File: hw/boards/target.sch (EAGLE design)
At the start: 21 parts, among them T1 771-BC847BS-T/R, U1 579-MCP1703T-3002ECB, U2 771-LPC824M201JDH20J, U4 579-MCP6291T-E/OT, X1 798-DF134P125V20

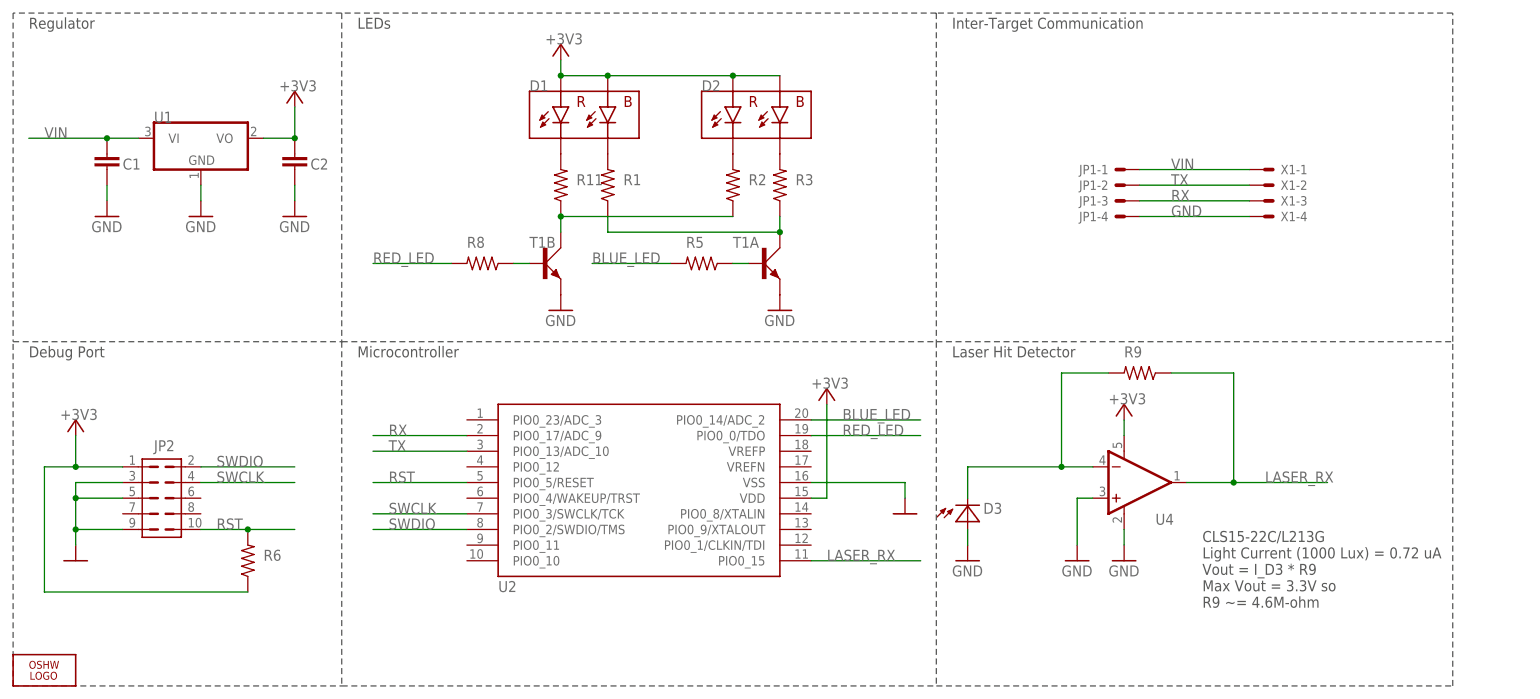
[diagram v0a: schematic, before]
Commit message: Cleanup some parts, generate BOM.
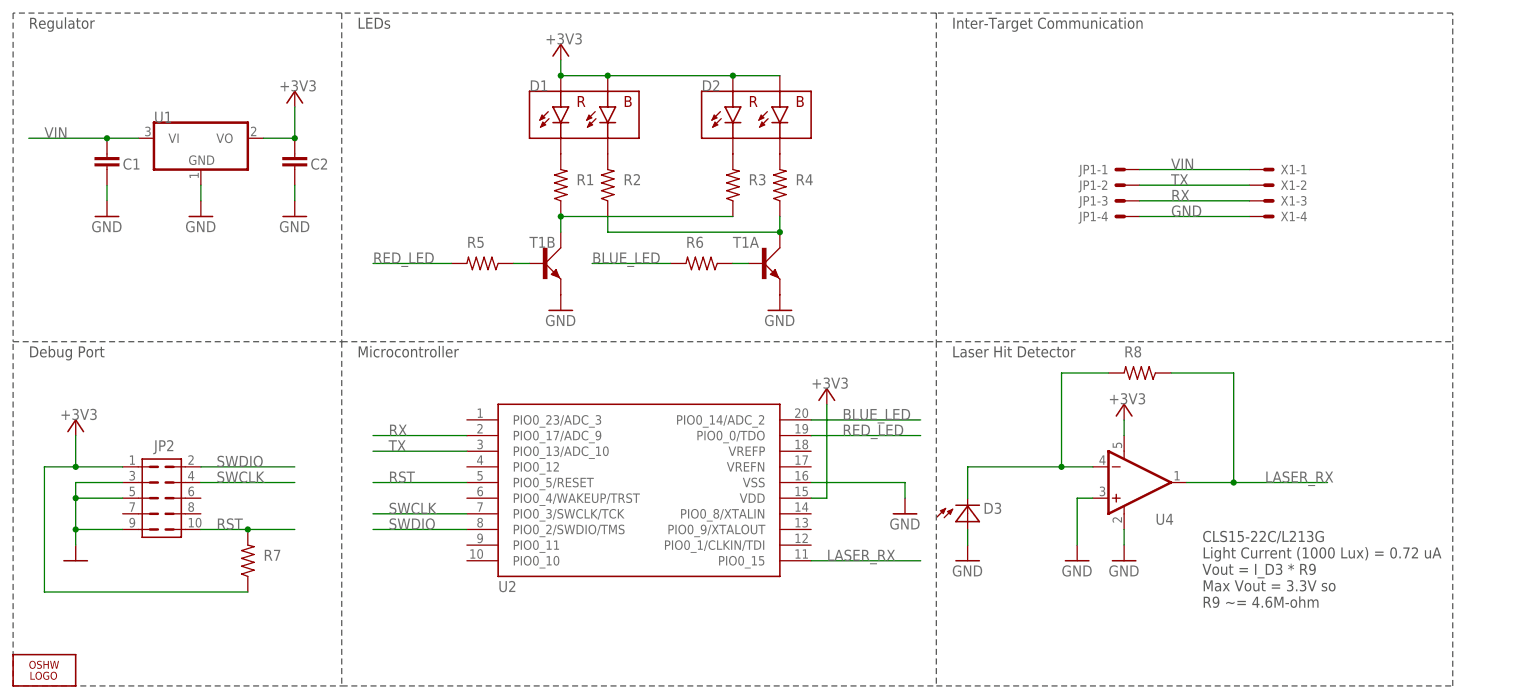
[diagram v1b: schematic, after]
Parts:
- removed R11: 71-CRCW060368R0FKEB, rcl:R-US_R0603
- removed R9: 71-CRCW06034M64FKEA, rcl:R-US_R0603
- added R4: 71-CRCW0603-5.6-E3, rcl:R-US_R0603
- added R7: 71-CRCW0603-10K-E3, rcl:R-US_R0603
- R1, R3: value 71-CRCW0603-5.6-E3 -> 71-CRCW060368R0FKEB
- R2: value 71-CRCW060368R0FKEB -> 71-CRCW0603-5.6-E3
- R6: value 71-CRCW0603-10K-E3 -> 71-CRCW0603220RFKEB
- R8: value 71-CRCW0603220RFKEB -> 71-CRCW06034M64FKEA
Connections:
- net +3V3: now also R7.1; no longer R6.1
- net BLUE_LED: now also R6.2; no longer R5.2
- net LASER_RX: now also R8.1; no longer R9.1
- net N$1: now also R2.1, R4.1; no longer R1.1, R3.1
- net N$11: now also R5.1; no longer R8.1
- net N$2: now also R1.1, R3.1; no longer R11.1, R2.1
- net N$3: now also R1.2; no longer R11.2
- net N$4: now also R6.1; no longer R5.1
- net N$5: now also R8.2; no longer R9.2
- net N$6: now also R3.2; no longer R2.2
- net N$7: now also R2.2; no longer R1.2
- net N$8: now also R4.2; no longer R3.2
- net RED_LED: now also R5.2; no longer R8.2
- net RST: now also R7.2; no longer R6.2
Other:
- moved on the sheet: R1, R2, R3, R5, R6, R8

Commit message: Fix some part numbers
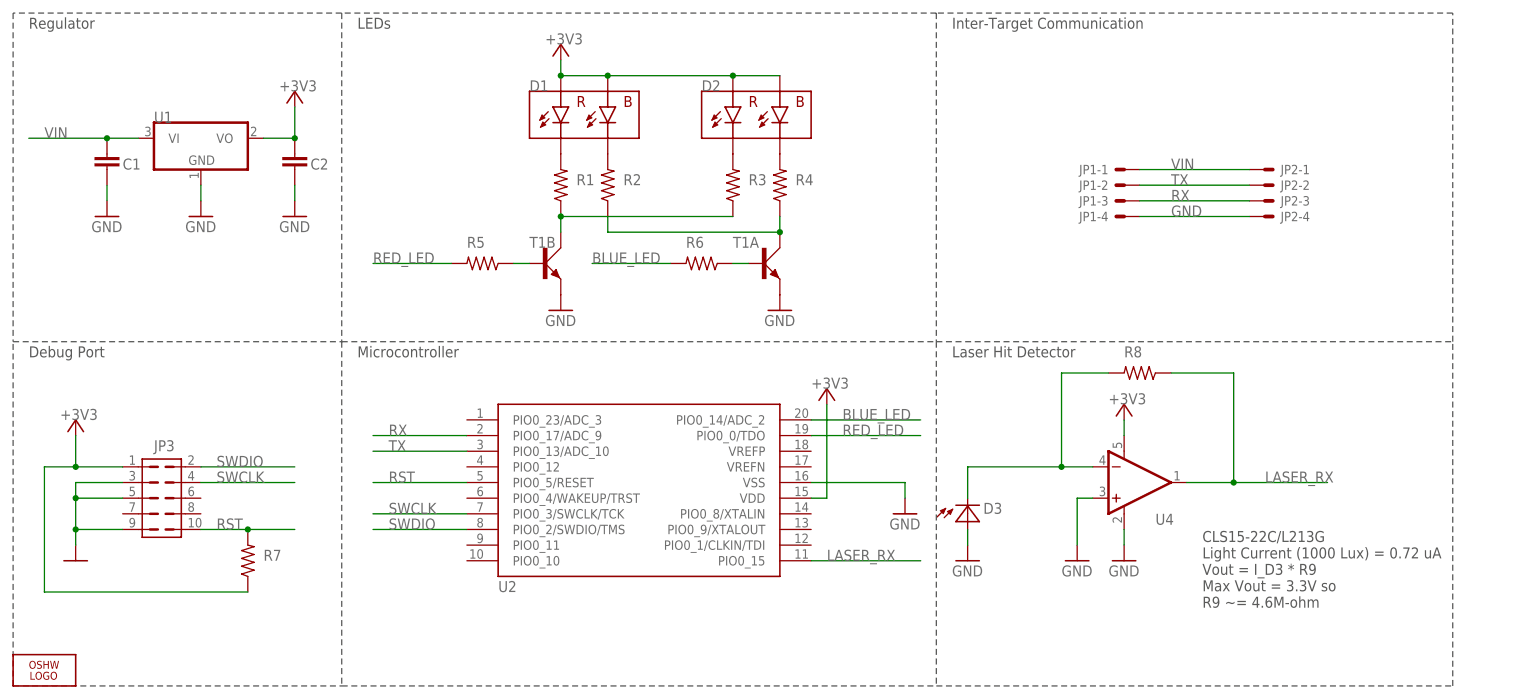
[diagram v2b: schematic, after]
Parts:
- removed X1: 798-DF134P125V20, con-molex:53398-04
- added JP3: FTSH-105-01-L, torpedo:FTSH-105
- JP2: value FTSH-105-01-L -> 798-DF134P125V20; device torpedo:FTSH-105 -> con-molex:53398-04
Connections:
- net +3V3: now also JP3.1; no longer JP2.1
- net GND: now also JP2-4.S, JP3.3, JP3.5, JP3.9; no longer JP2.3, JP2.5, JP2.9, X1-4.S
- net RST: now also JP3.10; no longer JP2.10
- net RX: now also JP2-3.S; no longer X1-3.S
- net SWCLK: now also JP3.4; no longer JP2.4
- net SWDIO: now also JP3.2; no longer JP2.2
- net TX: now also JP2-2.S; no longer X1-2.S
- net VIN: now also JP2-1.S; no longer X1-1.S
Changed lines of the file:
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@@
 <part name="R1" library="rcl" deviceset="R-US_" device="R0603" value="71-CRCW060368R0FKEB"/>
 <part name="T1" library="transistor-small-signal" deviceset="BC847BS" device="" value="771-BC847BS-T/R"/>
-<part name="X1" library="con-molex" deviceset="53?-04" device="398" value="798-DF134P125V20"/>
+<part name="JP2" library="con-molex" deviceset="53?-04" device="398" value="798-DF134P125V20"/>
 <part name="JP1" library="con-molex" deviceset="53?-04" device="398" value="798-DF134P125V20"/>
 <part name="LOGO2" library="ohw-logo" deviceset="OSHW_LOGO_FILL" device="X0150-NT"/>
@@
 <part name="GND8" library="supply1" deviceset="GND" device=""/>
 <part name="+3V31" library="supply1" deviceset="+3V3" device=""/>
-<part name="JP2" library="torpedo" deviceset="FTSH-105" device="" value="FTSH-105-01-L"/>
+<part name="JP3" library="torpedo" deviceset="FTSH-105" device="" value="FTSH-105-01-L"/>
 <part name="R7" library="rcl" deviceset="R-US_" device="R0603" value="71-CRCW0603-10K-E3"/>
 <part name="GND3" library="supply1" deviceset="GND" device=""/>
@@
 <attribute name="NAME" x="83.82" y="71.12" size="1.778" layer="95"/>
 </instance>
-<instance part="X1" gate="-1" x="203.2" y="83.82" smashed="yes">
+<instance part="JP2" gate="-1" x="203.2" y="83.82" smashed="yes">
 <attribute name="NAME" x="205.74" y="83.058" size="1.524" layer="95"/>
 </instance>
-<instance part="X1" gate="-2" x="203.2" y="81.28" smashed="yes">
+<instance part="JP2" gate="-2" x="203.2" y="81.28" smashed="yes">
 <attribute name="NAME" x="205.74" y="80.518" size="1.524" layer="95"/>
 </instance>
-<instance part="X1" gate="-3" x="203.2" y="78.74" smashed="yes">
+<instance part="JP2" gate="-3" x="203.2" y="78.74" smashed="yes">
 <attribute name="NAME" x="205.74" y="77.978" size="1.524" layer="95"/>
 </instance>
-<instance part="X1" gate="-4" x="203.2" y="76.2" smashed="yes">
+<instance part="JP2" gate="-4" x="203.2" y="76.2" smashed="yes">
 <attribute name="NAME" x="205.74" y="75.438" size="1.524" layer="95"/>
 </instance>
@@
 <attribute name="VALUE" x="7.62" y="43.18" size="1.778" layer="96"/>
 </instance>
-<instance part="JP2" gate="G$1" x="22.86" y="25.4" smashed="yes">
+<instance part="JP3" gate="G$1" x="22.86" y="25.4" smashed="yes">
 <attribute name="NAME" x="22.86" y="38.1" size="1.778" layer="95"/>
 </instance>
@@
 <segment>
 <pinref part="JP1" gate="-4" pin="S"/>
-<pinref part="X1" gate="-4" pin="S"/>
+<pinref part="JP2" gate="-4" pin="S"/>
 <wire x1="182.88" y1="76.2" x2="200.66" y2="76.2" width="0.1524" layer="91"/>
 <label x="187.96" y="76.2" size="1.778" layer="95"/>
 </segment>
 <segment>
-<pinref part="JP2" gate="G$1" pin="9"/>
+<pinref part="JP3" gate="G$1" pin="9"/>
 <pinref part="GND8" gate="1" pin="GND"/>
 <wire x1="17.78" y1="25.4" x2="10.16" y2="25.4" width="0.1524" layer="91"/>
 <wire x1="10.16" y1="25.4" x2="10.16" y2="22.86" width="0.1524" layer="91"/>
-<pinref part="JP2" gate="G$1" pin="5"/>
+<pinref part="JP3" gate="G$1" pin="5"/>
 <wire x1="17.78" y1="30.48" x2="10.16" y2="30.48" width="0.1524" layer="91"/>
 <wire x1="10.16" y1="30.48" x2="10.16" y2="25.4" width="0.1524" layer="91"/>
-<pinref part="JP2" gate="G$1" pin="3"/>
+<pinref part="JP3" gate="G$1" pin="3"/>
 <wire x1="17.78" y1="33.02" x2="10.16" y2="33.02" width="0.1524" layer="91"/>
 <wire x1="10.16" y1="33.02" x2="10.16" y2="30.48" width="0.1524" layer="91"/>
@@
 </segment>
 <segment>
-<pinref part="JP2" gate="G$1" pin="1"/>
+<pinref part="JP3" gate="G$1" pin="1"/>
 <pinref part="+3V31" gate="G$1" pin="+3V3"/>
 <wire x1="17.78" y1="35.56" x2="10.16" y2="35.56" width="0.1524" layer="91"/>
@@
 <label x="187.96" y="83.82" size="1.778" layer="95"/>
 <pinref part="JP1" gate="-1" pin="S"/>
-<pinref part="X1" gate="-1" pin="S"/>
+<pinref part="JP2" gate="-1" pin="S"/>
 </segment>
 </net>
@@
 <label x="187.96" y="81.28" size="1.778" layer="95"/>
 <pinref part="JP1" gate="-2" pin="S"/>
-<pinref part="X1" gate="-2" pin="S"/>
+<pinref part="JP2" gate="-2" pin="S"/>
 </segment>
 <segment>
@@
 </segment>
 <segment>
-<pinref part="JP2" gate="G$1" pin="2"/>
+<pinref part="JP3" gate="G$1" pin="2"/>
 <wire x1="30.48" y1="35.56" x2="45.72" y2="35.56" width="0.1524" layer="91"/>
 <label x="33.02" y="35.56" size="1.778" layer="95"/>
@@
 </segment>
 <segment>
-<pinref part="JP2" gate="G$1" pin="4"/>
+<pinref part="JP3" gate="G$1" pin="4"/>
 <wire x1="30.48" y1="33.02" x2="45.72" y2="33.02" width="0.1524" layer="91"/>
 <label x="33.02" y="33.02" size="1.778" layer="95"/>
@@
 </segment>
 <segment>
-<pinref part="JP2" gate="G$1" pin="10"/>
+<pinref part="JP3" gate="G$1" pin="10"/>
 <wire x1="30.48" y1="25.4" x2="38.1" y2="25.4" width="0.1524" layer="91"/>
 <label x="33.02" y="25.4" size="1.778" layer="95"/>
@@
 <label x="187.96" y="78.74" size="1.778" layer="95"/>
 <pinref part="JP1" gate="-3" pin="S"/>
-<pinref part="X1" gate="-3" pin="S"/>
-</segment>
-<segment>
+<pinref part="JP2" gate="-3" pin="S"/>
+</segment>
+<segment>
